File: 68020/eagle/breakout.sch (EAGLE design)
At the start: 5 parts, among them IC1 MC68020

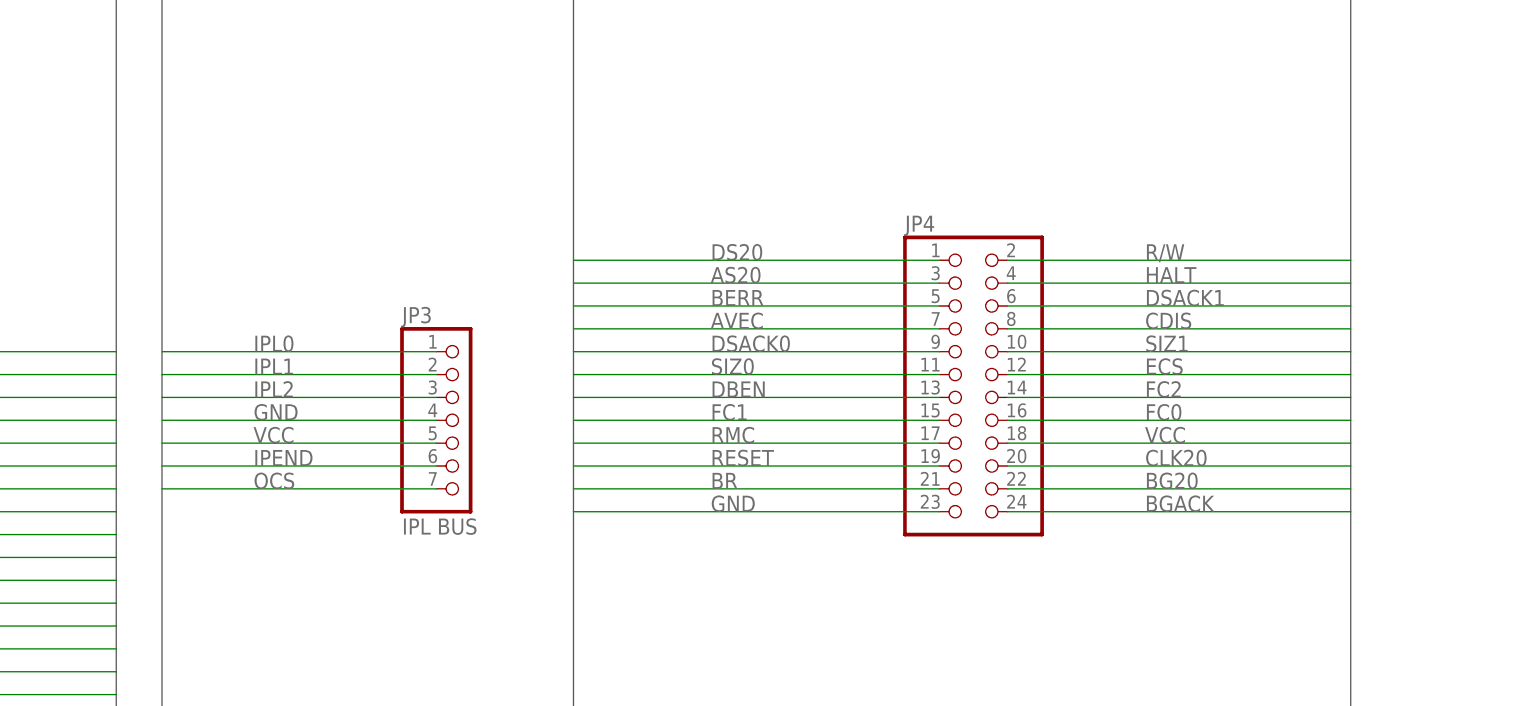
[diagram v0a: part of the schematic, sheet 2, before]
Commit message: refactored 68020 breakout board to be a mirror of the 030 board... means they can mate. Added an unrouted shunt for the 68k
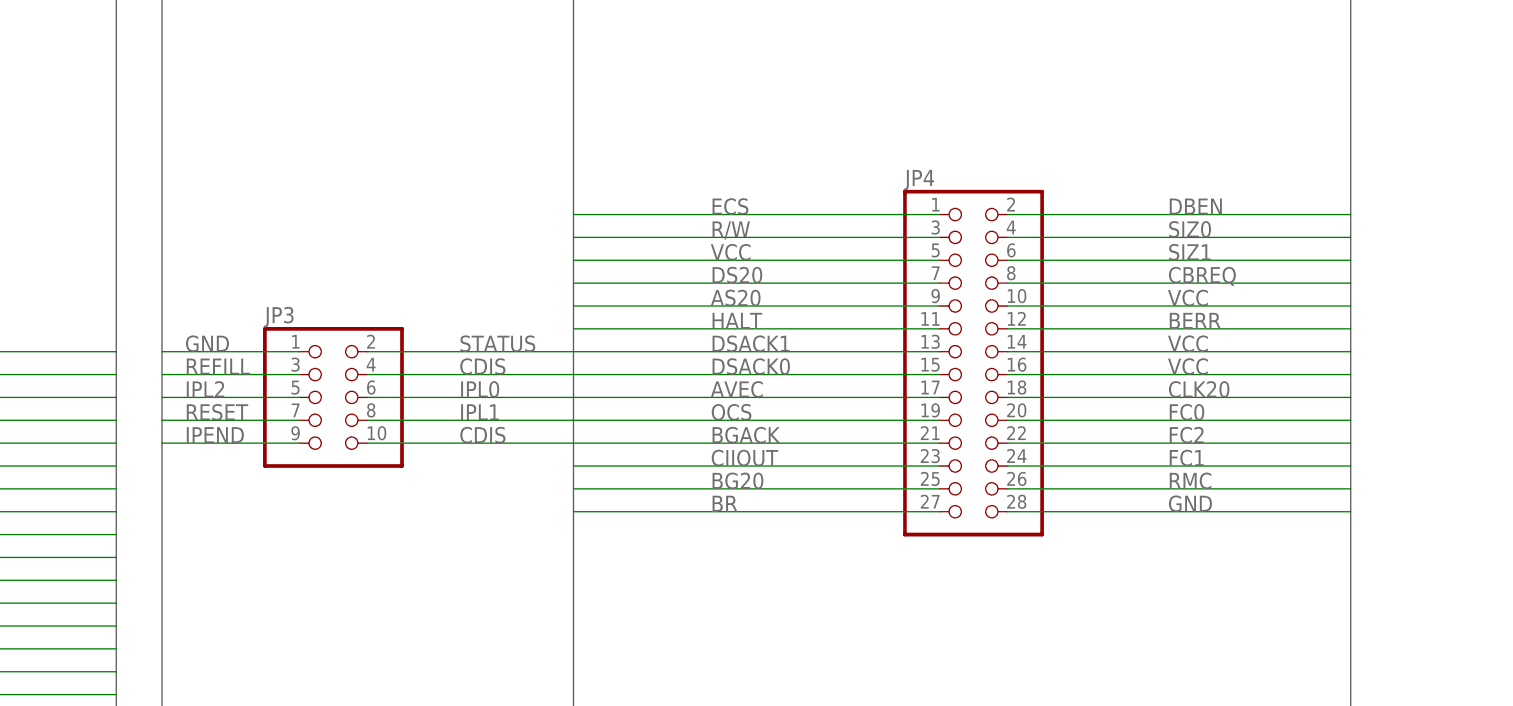
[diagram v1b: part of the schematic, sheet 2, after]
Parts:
- IC1: value MC68020 -> (none)
- JP3: value IPL BUS -> (none); device pinhead:PINHD-1X7 -> pinhead:PINHD-2X5
- JP4: device pinhead:PINHD-2X12 -> pinhead:PINHD-2X14
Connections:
- new net BG: IC1G$1.BG
- new net CBREQ: JP4.8
- new net CIIOUT: JP4.23
- new net REFILL: JP3.3
- new net STATUS: JP3.2
- net AS20: now also JP4.9; no longer JP4.3
- net AVEC: now also JP4.17; no longer JP4.7
- net BERR: now also JP4.12; no longer JP4.5
- net BG20: now also JP4.25; no longer IC1G$1.BG, JP4.22
- net BGACK: now also JP4.21; no longer JP4.24
- net BR: now also JP4.27; no longer JP4.21
- net CDIS: now also JP3.10, JP3.4; no longer JP4.8
- net CLK20: now also JP4.18; no longer JP4.20
- net DBEN: now also JP4.2; no longer JP4.13
- net DS20: now also JP4.7; no longer JP4.1
- net DSACK0: now also JP4.15; no longer JP4.9
- net DSACK1: now also JP4.13; no longer JP4.6
- net ECS: now also JP4.1; no longer JP4.12
- net FC0: now also JP4.20; no longer JP4.16
- net FC1: now also JP4.24; no longer JP4.15
- net FC2: now also JP4.22; no longer JP4.14
- net GND: now also JP3.1, JP4.28; no longer JP3.4, JP4.23
- net HALT: now also JP4.11; no longer JP4.4
- net IPEND: now also JP3.9; no longer JP3.6
- net IPL0: now also JP3.6; no longer JP3.1
- net IPL1: now also JP3.8; no longer JP3.2
- net IPL2: now also JP3.5; no longer JP3.3
- net OCS: now also JP4.19; no longer JP3.7
- net R/W: now also JP4.3; no longer JP4.2
- net RESET: now also JP3.7; no longer JP4.19
- net RMC: now also JP4.26; no longer JP4.17
- net SIZ0: now also JP4.4; no longer JP4.11
- net SIZ1: now also JP4.6; no longer JP4.10
- net VCC: now also JP4.10, JP4.14, JP4.16, JP4.5; no longer JP3.5, JP4.18
